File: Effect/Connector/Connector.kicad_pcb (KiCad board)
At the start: 2 copper layers, 30 x 84 mm, 20 parts, among them J1 Conn_01x04_Pin, J2 Conn_01x05_Pin, J4 RJ45_LED_Shielded, J5 USB_C_Receptacle_USB2.0_16P, U1 TLE2426xD, U2 OPA1656

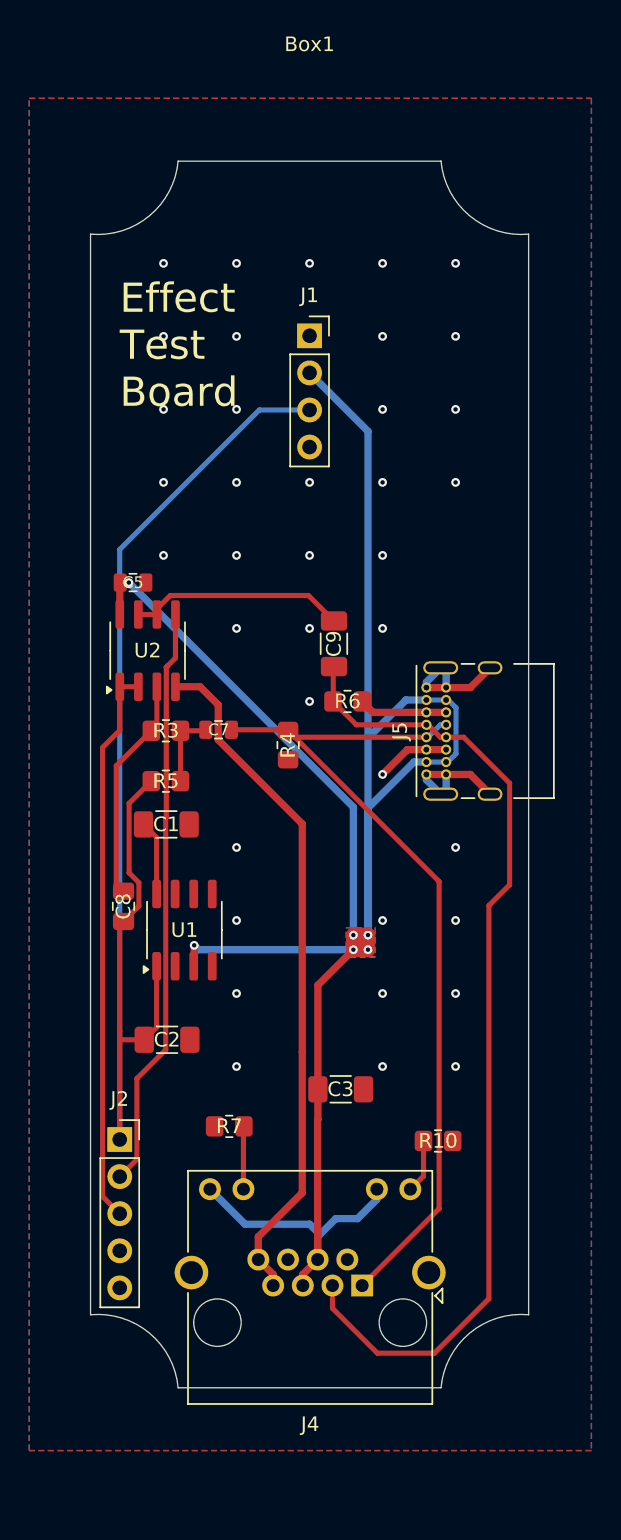
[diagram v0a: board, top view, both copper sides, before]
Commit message: Simplify the connector testing to just a USB-C connector
This is mainly to see what that would look like, particularly for the
base that now becomes really simple and small.

The effect connector ends up being crazy large just because of the old
pin header layout.  But the point of all this is that if it works out,
we'll dispense with the pin headers, and just use the USB-C connector
"natively".

So the effects board is just a temporary thing, and the base board is
where it's at.  If the base board works well, and I can stop soldering
stomp switches, I'll be good.

Signed-off-by: Linus Torvalds <torvalds@linux-foundation.org>
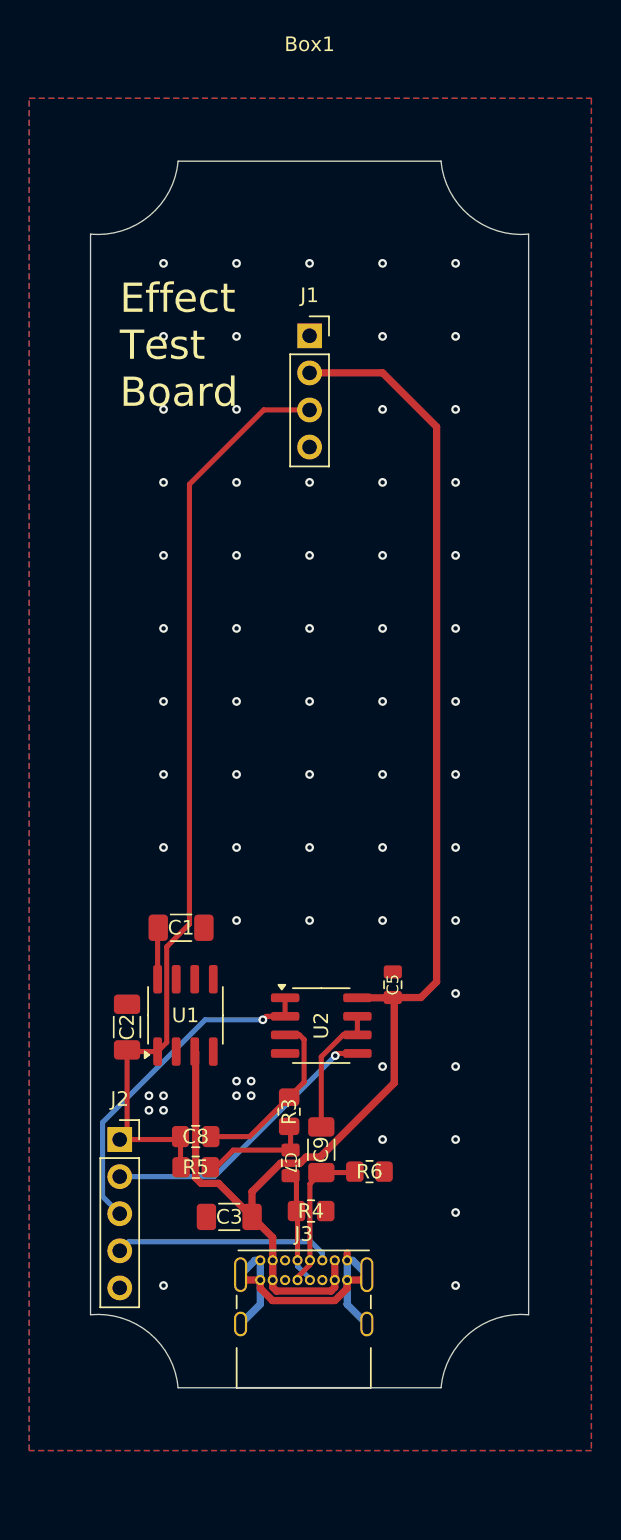
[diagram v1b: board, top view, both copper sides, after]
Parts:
- removed J4: RJ45_LED_Shielded, Connector_RJ:RJ45_Amphenol_RJHSE538X
- removed J5: USB_C_Receptacle_USB2.0_16P, Connector_USB:USB_C_Receptacle_GCT_USB4085
- removed R10, R7: 2.2k, Resistor_SMD:R_0805_2012Metric_Pad1.20x1.40mm_HandSolder
- added J3: USB_C_Receptacle_USB2.0_16P, Connector_USB:USB_C_Receptacle_GCT_USB4085, F.Cu at (96.6, 133.3)
- moved C9 34.7 mm to (100.8, 125.7)
- moved C5 32.8 mm to (105.7, 114.4), turned to 90 degrees
- moved R6 32.2 mm to (104.1, 127.2)
- moved R4 31.9 mm to (100.1, 129.9), turned to 0 degrees
- moved C7 30.1 mm to (98.7, 126.6), turned to 90 degrees
- moved U2 28.3 mm to (100.8, 117.2), turned to 0 degrees
- moved R3 27.4 mm to (98.6, 123.1), turned to 90 degrees
- moved R5 26.5 mm to (92.2, 126.9)
- moved C8 16.5 mm to (92.2, 124.8), turned to 180 degrees
- moved C3 11.6 mm to (94.5, 130.3), turned to 180 degrees
- moved C1 7.15 mm to (91.2, 110.5)
- moved U1 5.84 mm to (91.5, 116.5)
- moved C2 2.87 mm to (87.5, 117.3), turned to 90 degrees
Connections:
- J2 pad 4: GND -> ACTIVE
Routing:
- net OUT^{RAW}: track 67.4 -> 10.4 mm
- net +V: track 157.3 -> 100.6 mm, vias 6 -> 0
- net IN^{RAW}: track 59.7 -> 7.70 mm
- net GND: track 74.7 -> 24.6 mm, vias 38 -> 63
- net GNDREF: track 90.0 -> 64.9 mm
- net OUT^{EFF}: track 40.2 -> 19.8 mm, vias 0 -> 1
- net ACTIVE: track 0.00 -> 14.9 mm
- net IN^{EFF}: track 38.3 -> 23.5 mm, vias 0 -> 1
- net Net-(U2B--): track 14.5 -> 9.17 mm
- net Net-(J4-Pad11): track 4.31 -> 0.00 mm
- net Net-(J4-Pad9): track 3.67 -> 0.00 mm
- net Net-(C7-Pad2): track 5.11 -> 7.65 mm
- net Net-(U2A-+): track 14.8 -> 12.3 mm
- net Net-(U1-NOISE_REDUCTION): track 5.14 -> 3.54 mm
- removed copper zone on B.Cu, net +V
- removed copper zone on F.Cu, net +V
